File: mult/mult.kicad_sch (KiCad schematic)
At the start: 0 parts

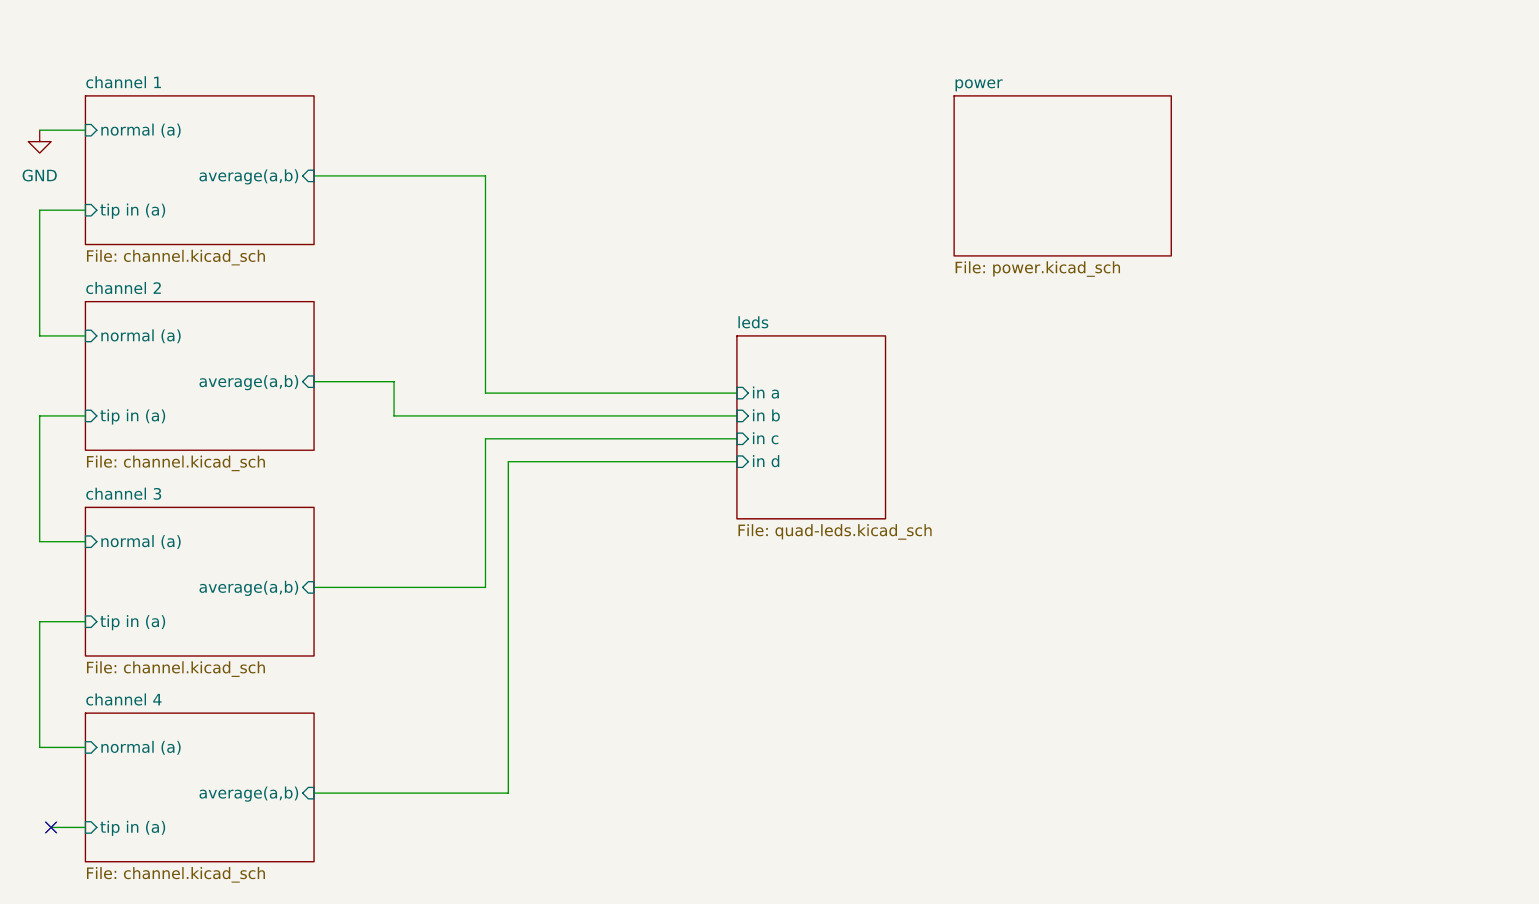
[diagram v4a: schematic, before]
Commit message: mult: Remove LEDs, add A-B output
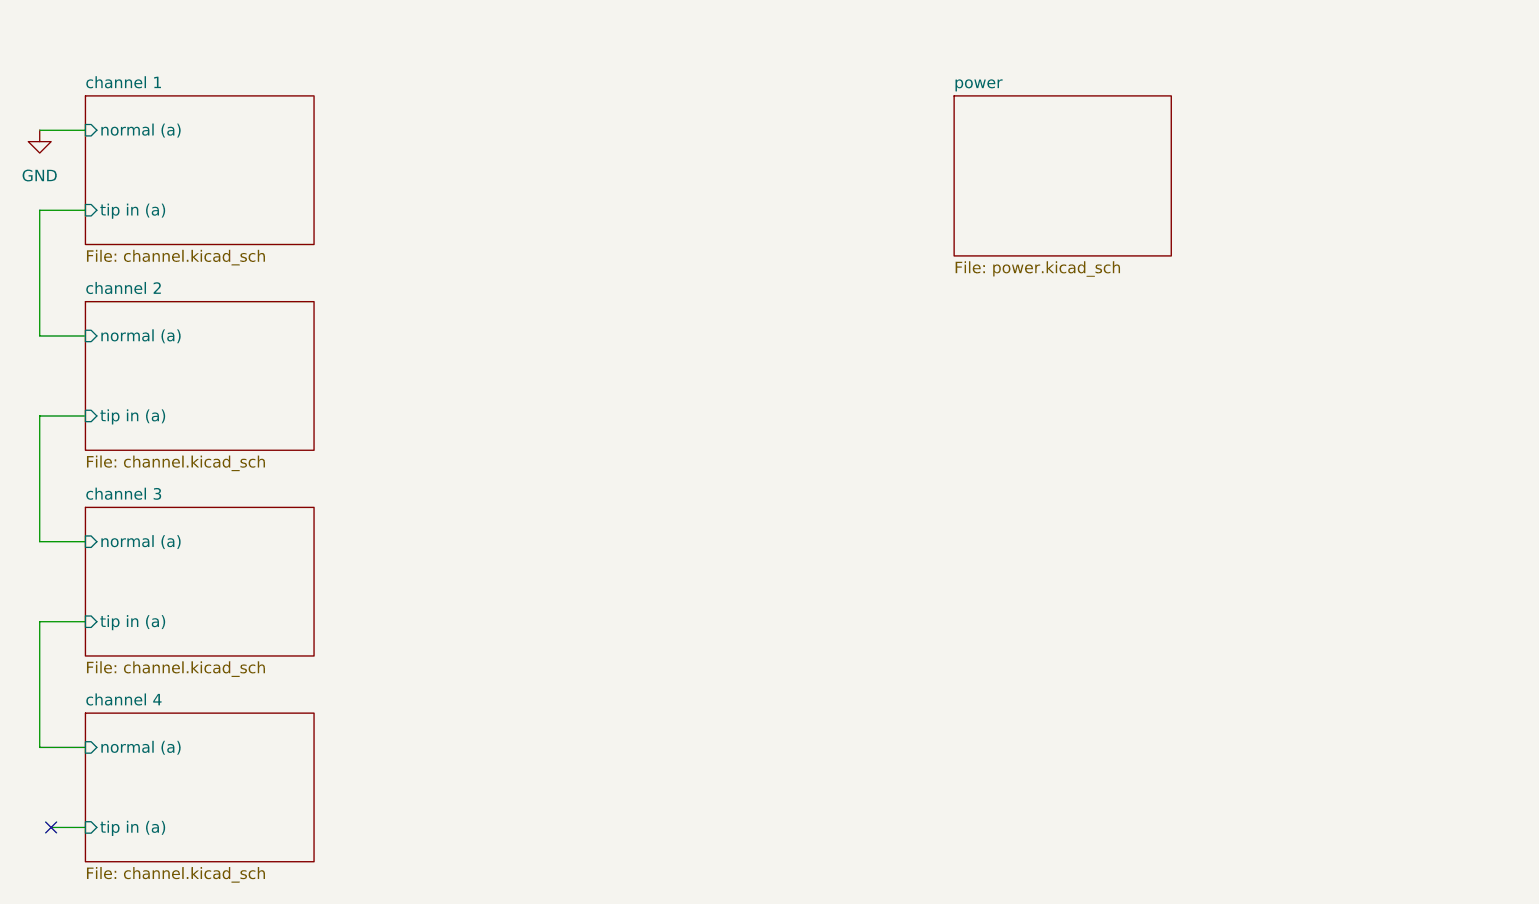
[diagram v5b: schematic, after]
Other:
- removed sheet leds
- sheet channel 1 ports: added none; removed average(a,b)
- sheet channel 2 ports: added none; removed average(a,b)
- sheet channel 3 ports: added none; removed average(a,b)
- sheet channel 4 ports: added none; removed average(a,b)
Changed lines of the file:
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@@
   (paper "A4")
   (no_connect (at 57.15 125.73))
-  (wire (pts (xy 107.95 121.92) (xy 86.36 121.92))
-    (stroke (width 0) (type default))
-  )
-  (wire (pts (xy 105.41 77.47) (xy 105.41 53.34))
-    (stroke (width 0) (type default))
-  )
   (wire (pts (xy 60.96 102.87) (xy 55.88 102.87))
     (stroke (width 0) (type default))
   )
-  (wire (pts (xy 95.25 80.01) (xy 95.25 76.2))
-    (stroke (width 0) (type default))
-  )
   (wire (pts (xy 57.15 125.73) (xy 60.96 125.73))
-    (stroke (width 0) (type default))
-  )
-  (wire (pts (xy 105.41 82.55) (xy 105.41 99.06))
-    (stroke (width 0) (type default))
-  )
-  (wire (pts (xy 133.35 80.01) (xy 95.25 80.01))
-    (stroke (width 0) (type default))
-  )
-  (wire (pts (xy 107.95 85.09) (xy 107.95 121.92))
     (stroke (width 0) (type default))
   )
@@
   )
   (wire (pts (xy 60.96 80.01) (xy 55.88 80.01))
-    (stroke (width 0) (type default))
-  )
-  (wire (pts (xy 105.41 99.06) (xy 86.36 99.06))
-    (stroke (width 0) (type default))
-  )
-  (wire (pts (xy 95.25 76.2) (xy 86.36 76.2))
-    (stroke (width 0) (type default))
-  )
-  (wire (pts (xy 133.35 77.47) (xy 105.41 77.47))
-    (stroke (width 0) (type default))
-  )
-  (wire (pts (xy 133.35 85.09) (xy 107.95 85.09))
     (stroke (width 0) (type default))
   )
@@
   )
   (wire (pts (xy 55.88 102.87) (xy 55.88 116.84))
-    (stroke (width 0) (type default))
-  )
-  (wire (pts (xy 105.41 53.34) (xy 86.36 53.34))
-    (stroke (width 0) (type default))
-  )
-  (wire (pts (xy 133.35 82.55) (xy 105.41 82.55))
     (stroke (width 0) (type default))
   )
@@
       (effects (font (size 1.27 1.27)) (justify left top))
     )
-    (pin "average(a,b)" input (at 86.36 53.34 0)
-      (effects (font (size 1.27 1.27)) (justify right))
-    )
     (pin "tip in (a)" input (at 60.96 57.15 180)
       (effects (font (size 1.27 1.27)) (justify left))
@@
       (project "mult"
         (path "/0e98ec4b-b4c7-447c-abd7-a761177a7f67" (page "2"))
-      )
-    )
-  )
-  (sheet (at 133.35 71.12) (size 16.51 20.32) (fields_autoplaced)
-    (stroke (width 0.1524) (type solid))
-    (fill (color 0 0 0 0.0000))
-    (property "Sheetname" "leds" (at 133.35 70.4084 0)
-      (effects (font (size 1.27 1.27)) (justify left bottom))
-    )
-    (property "Sheetfile" "quad-leds.kicad_sch" (at 133.35 92.0246 0)
-      (effects (font (size 1.27 1.27)) (justify left top))
-    )
-    (pin "in c" input (at 133.35 82.55 180)
-      (effects (font (size 1.27 1.27)) (justify left))
-    )
-    (pin "in a" input (at 133.35 77.47 180)
-      (effects (font (size 1.27 1.27)) (justify left))
-    )
-    (pin "in b" input (at 133.35 80.01 180)
-      (effects (font (size 1.27 1.27)) (justify left))
-    )
-    (pin "in d" input (at 133.35 85.09 180)
-      (effects (font (size 1.27 1.27)) (justify left))
-    )
-    (instances
-      (project "mult"
-        (path "/0e98ec4b-b4c7-447c-abd7-a761177a7f67" (page "6"))
       )
     )
@@
       (effects (font (size 1.27 1.27)) (justify left top))
     )
-    (pin "average(a,b)" input (at 86.36 99.06 0)
-      (effects (font (size 1.27 1.27)) (justify right))
-    )
     (pin "tip in (a)" input (at 60.96 102.87 180)
       (effects (font (size 1.27 1.27)) (justify left))
@@
     (property "Sheetfile" "channel.kicad_sch" (at 60.96 84.4046 0)
       (effects (font (size 1.27 1.27)) (justify left top))
-    )
-    (pin "average(a,b)" input (at 86.36 76.2 0)
-      (effects (font (size 1.27 1.27)) (justify right))
     )
     (pin "tip in (a)" input (at 60.96 80.01 180)
@@
       (effects (font (size 1.27 1.27)) (justify left top))
     )
-    (pin "average(a,b)" input (at 86.36 121.92 0)
-      (effects (font (size 1.27 1.27)) (justify right))
-    )
     (pin "normal (a)" input (at 60.96 116.84 180)
